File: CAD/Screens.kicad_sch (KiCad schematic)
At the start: 1 part

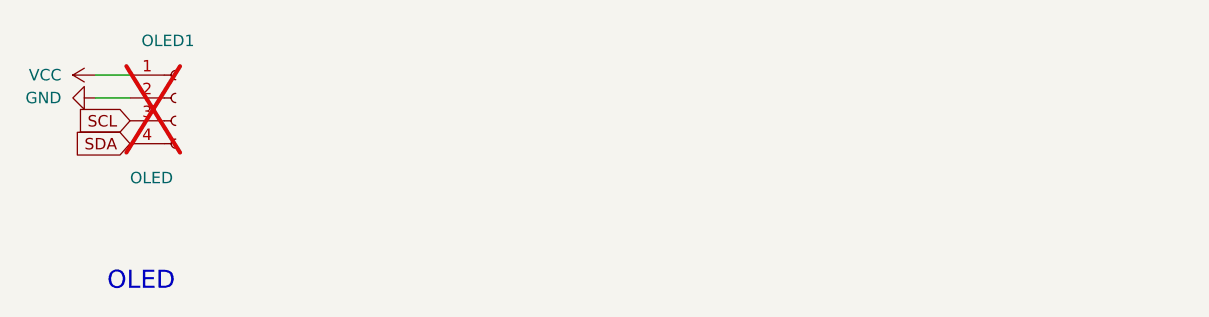
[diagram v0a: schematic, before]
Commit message: adding footprints and starting to route
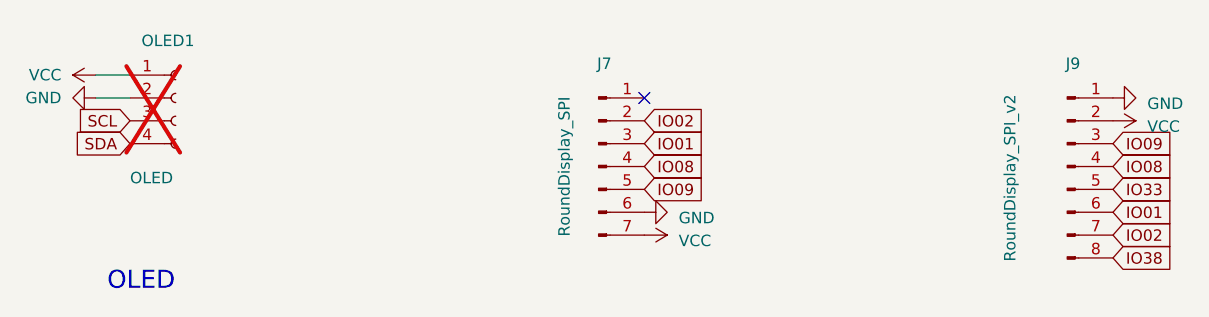
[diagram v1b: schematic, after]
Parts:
- added J7: RoundDisplay_SPI, Connector_PinSocket_2.54mm:PinSocket_1x07_P2.54mm_Vertical, symbol Connector:Conn_01x07_Pin
- added J9: RoundDisplay_SPI_v2, Connector_PinSocket_2.54mm:PinSocket_1x08_P2.54mm_Vertical, symbol Connector:Conn_01x08_Pin
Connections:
- net GND: now also J7.6 (Pin_6), J9.1 (Pin_1)
- net VCC: now also J7.7 (Pin_7), J9.2 (Pin_2)
- new net IO01: J7.3 (Pin_3), J9.6 (Pin_6)
- new net IO02: J7.2 (Pin_2), J9.7 (Pin_7)
- new net IO08: J7.4 (Pin_4), J9.4 (Pin_4)
- new net IO09: J7.5 (Pin_5), J9.3 (Pin_3)
- new net IO33: J9.5 (Pin_5)
- new net IO38: J9.8 (Pin_8)
- no-connect marks 0 -> 1
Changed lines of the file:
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@@
 (kicad_sch (version 20230121) (generator eeschema)
   (paper "A4")
+  (no_connect (at 133.35 69.85))
   (wire (pts (xy 72.39 67.31) (xy 76.2 67.31))
     (stroke (width 0) (type default))
@@
   (text "OLED" (at 73.66 91.44 0)
     (effects (font (size 2.0066 2.0066)) (justify left bottom))
+  )
+  (global_label "IO02" (shape input) (at 133.35 72.39 0) (fields_autoplaced)
+    (effects (font (size 1.27 1.27)) (justify left))
+    (property "Intersheetrefs" "${INTERSHEET_REFS}" (at 139.9559 72.39 0)
+      (effects (font (size 1.27 1.27)) (justify left) hide)
+    )
+  )
+  (global_label "IO38" (shape input) (at 185.42 87.63 0) (fields_autoplaced)
+    (effects (font (size 1.27 1.27)) (justify left))
+    (property "Intersheetrefs" "${INTERSHEET_REFS}" (at 192.0259 87.63 0)
+      (effects (font (size 1.27 1.27)) (justify left) hide)
+    )
+  )
+  (global_label "IO01" (shape input) (at 185.42 82.55 0) (fields_autoplaced)
+    (effects (font (size 1.27 1.27)) (justify left))
+    (property "Intersheetrefs" "${INTERSHEET_REFS}" (at 192.0259 82.55 0)
+      (effects (font (size 1.27 1.27)) (justify left) hide)
+    )
+  )
+  (global_label "IO09" (shape input) (at 185.42 74.93 0) (fields_autoplaced)
+    (effects (font (size 1.27 1.27)) (justify left))
+    (property "Intersheetrefs" "${INTERSHEET_REFS}" (at 192.0259 74.93 0)
+      (effects (font (size 1.27 1.27)) (justify left) hide)
+    )
   )
   (global_label "SDA" (shape input) (at 76.2 74.93 180) (fields_autoplaced)
@@
     )
   )
+  (global_label "IO08" (shape input) (at 133.35 77.47 0) (fields_autoplaced)
+    (effects (font (size 1.27 1.27)) (justify left))
+    (property "Intersheetrefs" "${INTERSHEET_REFS}" (at 139.9559 77.47 0)
+      (effects (font (size 1.27 1.27)) (justify left) hide)
+    )
+  )
+  (global_label "IO08" (shape input) (at 185.42 77.47 0) (fields_autoplaced)
+    (effects (font (size 1.27 1.27)) (justify left))
+    (property "Intersheetrefs" "${INTERSHEET_REFS}" (at 192.0259 77.47 0)
+      (effects (font (size 1.27 1.27)) (justify left) hide)
+    )
+  )
+  (global_label "IO01" (shape input) (at 133.35 74.93 0) (fields_autoplaced)
+    (effects (font (size 1.27 1.27)) (justify left))
+    (property "Intersheetrefs" "${INTERSHEET_REFS}" (at 139.9559 74.93 0)
+      (effects (font (size 1.27 1.27)) (justify left) hide)
+    )
+  )
   (global_label "SCL" (shape input) (at 76.2 72.39 180) (fields_autoplaced)
     (effects (font (size 1.27 1.27)) (justify right))
@@
     )
   )
+  (global_label "IO09" (shape input) (at 133.35 80.01 0) (fields_autoplaced)
+    (effects (font (size 1.27 1.27)) (justify left))
+    (property "Intersheetrefs" "${INTERSHEET_REFS}" (at 139.9559 80.01 0)
+      (effects (font (size 1.27 1.27)) (justify left) hide)
+    )
+  )
+  (global_label "IO33" (shape input) (at 185.42 80.01 0) (fields_autoplaced)
+    (effects (font (size 1.27 1.27)) (justify left))
+    (property "Intersheetrefs" "${INTERSHEET_REFS}" (at 192.0259 80.01 0)
+      (effects (font (size 1.27 1.27)) (justify left) hide)
+    )
+  )
+  (global_label "IO02" (shape input) (at 185.42 85.09 0) (fields_autoplaced)
+    (effects (font (size 1.27 1.27)) (justify left))
+    (property "Intersheetrefs" "${INTERSHEET_REFS}" (at 192.0259 85.09 0)
+      (effects (font (size 1.27 1.27)) (justify left) hide)
+    )
+  )
+  (symbol (lib_name "VCC_1") (lib_id "power:VCC") (at 185.42 72.39 270) (unit 1)
+    (in_bom yes) (on_board yes) (dnp no) (fields_autoplaced)
+    (property "Reference" "#PWR068" (at 181.61 72.39 0)
+      (effects (font (size 1.27 1.27)) hide)
+    )
+    (property "Value" "VCC" (at 189.23 73.025 90)
+      (effects (font (size 1.27 1.27)) (justify left))
+    )
+    (property "Footprint" "" (at 185.42 72.39 0)
+      (effects (font (size 1.27 1.27)) hide)
+    )
+    (property "Datasheet" "" (at 185.42 72.39 0)
+      (effects (font (size 1.27 1.27)) hide)
+    )
+    (pin "1")
+    (instances
+      (project "ProjectNeoRogue"
+        (path "/76a22395-5d2d-4f66-8191-432f65fdc4ac/7bbc5ee4-a356-48de-a261-211ab35ec87b"
+          (reference "#PWR068") (unit 1)
+        )
+      )
+    )
+  )
+  (symbol (lib_id "Connector:Conn_01x08_Pin") (at 180.34 77.47 0) (unit 1)
+    (in_bom yes) (on_board yes) (dnp no)
+    (property "Reference" "J9" (at 180.975 66.04 0)
+      (effects (font (size 1.27 1.27)))
+    )
+    (property "Value" "RoundDisplay_SPI_v2" (at 173.99 78.74 90)
+      (effects (font (size 1.27 1.27)))
+    )
+    (property "Footprint" "Connector_PinSocket_2.54mm:PinSocket_1x08_P2.54mm_Vertical" (at 180.34 77.47 0)
+      (effects (font (size 1.27 1.27)) hide)
+    )
+    (property "Datasheet" "~" (at 180.34 77.47 0)
+      (effects (font (size 1.27 1.27)) hide)
+    )
+    (pin "1")
+    (pin "2")
+    (pin "3")
+    (pin "4")
+    (pin "5")
+    (pin "6")
+    (pin "7")
+    (pin "8")
+    (instances
+      (project "ProjectNeoRogue"
+        (path "/76a22395-5d2d-4f66-8191-432f65fdc4ac/7bbc5ee4-a356-48de-a261-211ab35ec87b"
+          (reference "J9") (unit 1)
+        )
+      )
+    )
+  )
+  (symbol (lib_id "Connector:Conn_01x07_Pin") (at 128.27 77.47 0) (unit 1)
+    (in_bom yes) (on_board yes) (dnp no)
+    (property "Reference" "J7" (at 128.905 66.04 0)
+      (effects (font (size 1.27 1.27)))
+    )
+    (property "Value" "RoundDisplay_SPI" (at 124.46 77.47 90)
+      (effects (font (size 1.27 1.27)))
+    )
+    (property "Footprint" "Connector_PinSocket_2.54mm:PinSocket_1x07_P2.54mm_Vertical" (at 128.27 77.47 0)
+      (effects (font (size 1.27 1.27)) hide)
+    )
+    (property "Datasheet" "~" (at 128.27 77.47 0)
+      (effects (font (size 1.27 1.27)) hide)
+    )
+    (pin "1")
+    (pin "2")
+    (pin "3")
+    (pin "4")
+    (pin "5")
+    (pin "6")
+    (pin "7")
+    (instances
+      (project "ProjectNeoRogue"
+        (path "/76a22395-5d2d-4f66-8191-432f65fdc4ac/7bbc5ee4-a356-48de-a261-211ab35ec87b"
+          (reference "J7") (unit 1)
+        )
+      )
+    )
+  )
   (symbol (lib_id "power:GND") (at 72.39 69.85 270) (unit 1)
     (in_bom yes) (on_board yes) (dnp no) (fields_autoplaced)
@@
     )
   )
+  (symbol (lib_name "GND_1") (lib_id "power:GND") (at 133.35 82.55 90) (unit 1)
+    (in_bom yes) (on_board yes) (dnp no) (fields_autoplaced)
+    (property "Reference" "#PWR065" (at 139.7 82.55 0)
+      (effects (font (size 1.27 1.27)) hide)
+    )
+    (property "Value" "GND" (at 137.16 83.185 90)
+      (effects (font (size 1.27 1.27)) (justify right))
+    )
+    (property "Footprint" "" (at 133.35 82.55 0)
+      (effects (font (size 1.27 1.27)) hide)
+    )
+    (property "Datasheet" "" (at 133.35 82.55 0)
+      (effects (font (size 1.27 1.27)) hide)
+    )
+    (pin "1")
+    (instances
+      (project "ProjectNeoRogue"
+        (path "/76a22395-5d2d-4f66-8191-432f65fdc4ac/7bbc5ee4-a356-48de-a261-211ab35ec87b"
+          (reference "#PWR065") (unit 1)
+        )
+      )
+    )
+  )
   (symbol (lib_id "power:VCC") (at 72.39 67.31 90) (unit 1)
     (in_bom yes) (on_board yes) (dnp no) (fields_autoplaced)
@@
         )
       )
+    )
+  )
+  (symbol (lib_name "VCC_1") (lib_id "power:VCC") (at 133.35 85.09 270) (unit 1)
+    (in_bom yes) (on_board yes) (dnp no) (fields_autoplaced)
+    (property "Reference" "#PWR066" (at 129.54 85.09 0)
+      (effects (font (size 1.27 1.27)) hide)
+    )
+    (property "Value" "VCC" (at 137.16 85.725 90)
+      (effects (font (size 1.27 1.27)) (justify left))
+    )
+    (property "Footprint" "" (at 133.35 85.09 0)
+      (effects (font (size 1.27 1.27)) hide)
+    )
+    (property "Datasheet" "" (at 133.35 85.09 0)
+      (effects (font (size 1.27 1.27)) hide)
+    )
+    (pin "1")
+    (instances
+      (project "ProjectNeoRogue"
+        (path "/76a22395-5d2d-4f66-8191-432f65fdc4ac/7bbc5ee4-a356-48de-a261-211ab35ec87b"
+          (reference "#PWR066") (unit 1)
+        )
+      )
+    )
+  )
+  (symbol (lib_name "GND_1") (lib_id "power:GND") (at 185.42 69.85 90) (unit 1)
+    (in_bom yes) (on_board yes) (dnp no) (fields_autoplaced)
+    (property "Reference" "#PWR067" (at 191.77 69.85 0)
+      (effects (font (size 1.27 1.27)) hide)
+    )
+    (property "Value" "GND" (at 189.23 70.485 90)
+      (effects (font (size 1.27 1.27)) (justify right))
+    )
+    (property "Footprint" "" (at 185.42 69.85 0)
+      (effects (font (size 1.27 1.27)) hide)
+    )
+    (property "Datasheet" "" (at 185.42 69.85 0)
+      (effects (font (size 1.27 1.27)) hide)
+    )
+    (pin "1")
+    (instances
+      (project "ProjectNeoRogue"
+        (path "/76a22395-5d2d-4f66-8191-432f65fdc4ac/7bbc5ee4-a356-48de-a261-211ab35ec87b"
+          (reference "#PWR067") (unit 1)
+        )
+      )

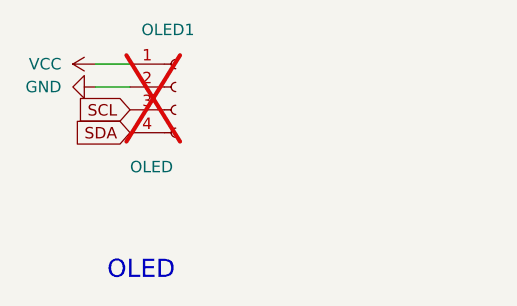
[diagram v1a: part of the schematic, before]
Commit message: routing and removing buttons OLED
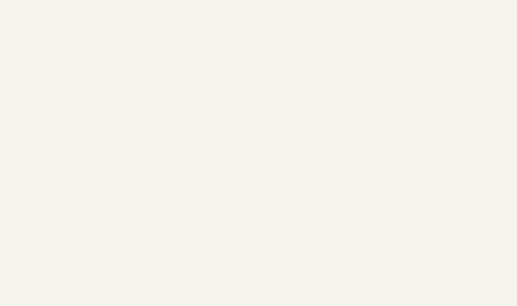
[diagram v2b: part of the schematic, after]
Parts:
- removed OLED1: OLED, Connector_PinHeader_2.54mm:PinHeader_1x04_P2.54mm_Vertical, symbol Connector:Conn_01x04_Female
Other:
- note removed: "OLED"
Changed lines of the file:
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@@
   (paper "A4")
   (no_connect (at 133.35 69.85))
-  (wire (pts (xy 72.39 67.31) (xy 76.2 67.31))
-    (stroke (width 0) (type default))
-  )
-  (wire (pts (xy 72.39 69.85) (xy 76.2 69.85))
-    (stroke (width 0) (type default))
-  )
-  (text "OLED" (at 73.66 91.44 0)
-    (effects (font (size 2.0066 2.0066)) (justify left bottom))
-  )
   (global_label "IO02" (shape input) (at 133.35 72.39 0) (fields_autoplaced)
     (effects (font (size 1.27 1.27)) (justify left))
@@
     )
   )
-  (global_label "SDA" (shape input) (at 76.2 74.93 180) (fields_autoplaced)
-    (effects (font (size 1.27 1.27)) (justify right))
-    (property "Intersheetrefs" "${INTERSHEET_REFS}" (at 70.2188 74.8506 0)
-      (effects (font (size 1.27 1.27)) (justify right) hide)
-    )
-  )
   (global_label "IO08" (shape input) (at 133.35 77.47 0) (fields_autoplaced)
     (effects (font (size 1.27 1.27)) (justify left))
@@
     (property "Intersheetrefs" "${INTERSHEET_REFS}" (at 139.9559 74.93 0)
       (effects (font (size 1.27 1.27)) (justify left) hide)
-    )
-  )
-  (global_label "SCL" (shape input) (at 76.2 72.39 180) (fields_autoplaced)
-    (effects (font (size 1.27 1.27)) (justify right))
-    (property "Intersheetrefs" "${INTERSHEET_REFS}" (at 70.2793 72.3106 0)
-      (effects (font (size 1.27 1.27)) (justify right) hide)
     )
   )
@@
     )
   )
-  (symbol (lib_id "power:GND") (at 72.39 69.85 270) (unit 1)
-    (in_bom yes) (on_board yes) (dnp no) (fields_autoplaced)
-    (property "Reference" "#PWR023" (at 66.04 69.85 0)
-      (effects (font (size 1.27 1.27)) hide)
-    )
-    (property "Value" "GND" (at 68.58 69.8499 90)
-      (effects (font (size 1.27 1.27)) (justify right))
-    )
-    (property "Footprint" "" (at 72.39 69.85 0)
-      (effects (font (size 1.27 1.27)) hide)
-    )
-    (property "Datasheet" "" (at 72.39 69.85 0)
-      (effects (font (size 1.27 1.27)) hide)
-    )
-    (pin "1")
-    (instances
-      (project "ProjectNeoRogue"
-        (path "/76a22395-5d2d-4f66-8191-432f65fdc4ac"
-          (reference "#PWR023") (unit 1)
-        )
-        (path "/76a22395-5d2d-4f66-8191-432f65fdc4ac/7bbc5ee4-a356-48de-a261-211ab35ec87b"
-          (reference "#PWR023") (unit 1)
-        )
-      )
-    )
-  )
-  (symbol (lib_id "Connector:Conn_01x04_Female") (at 81.28 69.85 0) (unit 1)
-    (in_bom no) (on_board yes) (dnp yes)
-    (property "Reference" "OLED1" (at 77.47 63.5 0)
-      (effects (font (size 1.27 1.27)) (justify left))
-    )
-    (property "Value" "OLED" (at 76.2 78.74 0)
-      (effects (font (size 1.27 1.27)) (justify left))
-    )
-    (property "Footprint" "Connector_PinHeader_2.54mm:PinHeader_1x04_P2.54mm_Vertical" (at 81.28 69.85 0)
-      (effects (font (size 1.27 1.27)) hide)
-    )
-    (property "Datasheet" "~" (at 81.28 69.85 0)
-      (effects (font (size 1.27 1.27)) hide)
-    )
-    (property "OrderURL" "" (at 81.28 69.85 0)
-      (effects (font (size 1.27 1.27)) hide)
-    )
-    (pin "1")
-    (pin "2")
-    (pin "3")
-    (pin "4")
-    (instances
-      (project "ProjectNeoRogue"
-        (path "/76a22395-5d2d-4f66-8191-432f65fdc4ac"
-          (reference "OLED1") (unit 1)
-        )
-        (path "/76a22395-5d2d-4f66-8191-432f65fdc4ac/7bbc5ee4-a356-48de-a261-211ab35ec87b"
-          (reference "OLED1") (unit 1)
-        )
-      )
-    )
-  )
   (symbol (lib_name "GND_1") (lib_id "power:GND") (at 133.35 82.55 90) (unit 1)
     (in_bom yes) (on_board yes) (dnp no) (fields_autoplaced)
@@
         )
       )
-    )
-  )
-  (symbol (lib_id "power:VCC") (at 72.39 67.31 90) (unit 1)
-    (in_bom yes) (on_board yes) (dnp no) (fields_autoplaced)
-    (property "Reference" "#PWR022" (at 76.2 67.31 0)
-      (effects (font (size 1.27 1.27)) hide)
-    )
-    (property "Value" "VCC" (at 68.58 67.3099 90)
-      (effects (font (size 1.27 1.27)) (justify left))
-    )
-    (property "Footprint" "" (at 72.39 67.31 0)
-      (effects (font (size 1.27 1.27)) hide)
-    )
-    (property "Datasheet" "" (at 72.39 67.31 0)
-      (effects (font (size 1.27 1.27)) hide)
-    )
-    (pin "1")
-    (instances
-      (project "ProjectNeoRogue"
-        (path "/76a22395-5d2d-4f66-8191-432f65fdc4ac"
-          (reference "#PWR022") (unit 1)
-        )
-        (path "/76a22395-5d2d-4f66-8191-432f65fdc4ac/7bbc5ee4-a356-48de-a261-211ab35ec87b"
-          (reference "#PWR022") (unit 1)
-        )
-      )

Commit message: Updated pins and moar
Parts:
- added R25 (x2): 4.7k, BadgePirates:R_1206_3216Metric, symbol Device:R_Small_US
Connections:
- net IO08: now also R25.2
- net IO09: now also R25.2
- net VCC: now also R25.1, R25.1
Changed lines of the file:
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@@
 (kicad_sch (version 20230121) (generator eeschema)
   (paper "A4")
+  (junction (at 153.67 80.01) (diameter 0) (color 0 0 0 0)
+  )
+  (junction (at 144.78 77.47) (diameter 0) (color 0 0 0 0)
+  )
   (no_connect (at 133.35 69.85))
+  (wire (pts (xy 153.67 66.675) (xy 153.67 69.85))
+    (stroke (width 0) (type default))
+  )
+  (wire (pts (xy 144.78 75.565) (xy 144.78 77.47))
+    (stroke (width 0) (type default))
+  )
+  (wire (pts (xy 153.67 74.93) (xy 153.67 80.01))
+    (stroke (width 0) (type default))
+  )
+  (wire (pts (xy 144.78 67.31) (xy 144.78 70.485))
+    (stroke (width 0) (type default))
+  )
+  (wire (pts (xy 153.67 80.01) (xy 133.35 80.01))
+    (stroke (width 0) (type default))
+  )
+  (wire (pts (xy 158.115 80.01) (xy 153.67 80.01))
+    (stroke (width 0) (type default))
+  )
+  (wire (pts (xy 144.78 77.47) (xy 133.35 77.47))
+    (stroke (width 0) (type default))
+  )
+  (wire (pts (xy 158.115 77.47) (xy 144.78 77.47))
+    (stroke (width 0) (type default))
+  )
   (global_label "IO02" (shape input) (at 133.35 72.39 0) (fields_autoplaced)
     (effects (font (size 1.27 1.27)) (justify left))
@@
     )
   )
-  (global_label "IO08" (shape input) (at 133.35 77.47 0) (fields_autoplaced)
-    (effects (font (size 1.27 1.27)) (justify left))
-    (property "Intersheetrefs" "${INTERSHEET_REFS}" (at 139.9559 77.47 0)
+  (global_label "IO08" (shape input) (at 158.115 77.47 0) (fields_autoplaced)
+    (effects (font (size 1.27 1.27)) (justify left))
+    (property "Intersheetrefs" "${INTERSHEET_REFS}" (at 164.7209 77.47 0)
       (effects (font (size 1.27 1.27)) (justify left) hide)
     )
@@
     )
   )
-  (global_label "IO09" (shape input) (at 133.35 80.01 0) (fields_autoplaced)
-    (effects (font (size 1.27 1.27)) (justify left))
-    (property "Intersheetrefs" "${INTERSHEET_REFS}" (at 139.9559 80.01 0)
+  (global_label "IO09" (shape input) (at 158.115 80.01 0) (fields_autoplaced)
+    (effects (font (size 1.27 1.27)) (justify left))
+    (property "Intersheetrefs" "${INTERSHEET_REFS}" (at 164.7209 80.01 0)
       (effects (font (size 1.27 1.27)) (justify left) hide)
     )
@@
         (path "/76a22395-5d2d-4f66-8191-432f65fdc4ac/7bbc5ee4-a356-48de-a261-211ab35ec87b"
           (reference "#PWR068") (unit 1)
+        )
+      )
+    )
+  )
+  (symbol (lib_id "power:VCC") (at 144.78 67.31 0) (unit 1)
+    (in_bom yes) (on_board yes) (dnp no)
+    (property "Reference" "#PWR027" (at 144.78 71.12 0)
+      (effects (font (size 1.27 1.27)) hide)
+    )
+    (property "Value" "VCC" (at 145.161 62.9158 0)
+      (effects (font (size 1.27 1.27)))
+    )
+    (property "Footprint" "" (at 144.78 67.31 0)
+      (effects (font (size 1.27 1.27)) hide)
+    )
+    (property "Datasheet" "" (at 144.78 67.31 0)
+      (effects (font (size 1.27 1.27)) hide)
+    )
+    (pin "1")
+    (instances
+      (project "ProjectNeoRogue"
+        (path "/76a22395-5d2d-4f66-8191-432f65fdc4ac"
+          (reference "#PWR027") (unit 1)
+        )
+        (path "/76a22395-5d2d-4f66-8191-432f65fdc4ac/7bbc5ee4-a356-48de-a261-211ab35ec87b"
+          (reference "#PWR028") (unit 1)
         )
       )
@@
     )
   )
+  (symbol (lib_id "Device:R_Small_US") (at 153.67 72.39 0) (unit 1)
+    (in_bom yes) (on_board yes) (dnp no)
+    (property "Reference" "R25" (at 155.3972 71.2216 0)
+      (effects (font (size 1.27 1.27)) (justify left))
+    )
+    (property "Value" "4.7k" (at 155.3972 73.533 0)
+      (effects (font (size 1.27 1.27)) (justify left))
+    )
+    (property "Footprint" "BadgePirates:R_1206_3216Metric" (at 153.67 72.39 0)
+      (effects (font (size 1.27 1.27)) hide)
+    )
+    (property "Datasheet" "~" (at 153.67 72.39 0)
+      (effects (font (size 1.27 1.27)) hide)
+    )
+    (property "OrderURL" "" (at 153.67 72.39 0)
+      (effects (font (size 1.27 1.27)) hide)
+    )
+    (pin "1")
+    (pin "2")
+    (instances
+      (project "ProjectNeoRogue"
+        (path "/76a22395-5d2d-4f66-8191-432f65fdc4ac"
+          (reference "R25") (unit 1)
+        )
+        (path "/76a22395-5d2d-4f66-8191-432f65fdc4ac/7bbc5ee4-a356-48de-a261-211ab35ec87b"
+          (reference "R27") (unit 1)
+        )
+      )
+    )
+  )
+  (symbol (lib_id "Device:R_Small_US") (at 144.78 73.025 0) (unit 1)
+    (in_bom yes) (on_board yes) (dnp no)
+    (property "Reference" "R25" (at 146.5072 71.8566 0)
+      (effects (font (size 1.27 1.27)) (justify left))
+    )
+    (property "Value" "4.7k" (at 146.5072 74.168 0)
+      (effects (font (size 1.27 1.27)) (justify left))
+    )
+    (property "Footprint" "BadgePirates:R_1206_3216Metric" (at 144.78 73.025 0)
+      (effects (font (size 1.27 1.27)) hide)
+    )
+    (property "Datasheet" "~" (at 144.78 73.025 0)
+      (effects (font (size 1.27 1.27)) hide)
+    )
+    (property "OrderURL" "" (at 144.78 73.025 0)
+      (effects (font (size 1.27 1.27)) hide)
+    )
+    (pin "1")
+    (pin "2")
+    (instances
+      (project "ProjectNeoRogue"
+        (path "/76a22395-5d2d-4f66-8191-432f65fdc4ac"
+          (reference "R25") (unit 1)
+        )
+        (path "/76a22395-5d2d-4f66-8191-432f65fdc4ac/7bbc5ee4-a356-48de-a261-211ab35ec87b"
+          (reference "R23") (unit 1)
+        )
+      )
+    )
+  )
   (symbol (lib_name "GND_1") (lib_id "power:GND") (at 133.35 82.55 90) (unit 1)
     (in_bom yes) (on_board yes) (dnp no) (fields_autoplaced)
@@
         )
       )
+    )
+  )
+  (symbol (lib_id "power:VCC") (at 153.67 66.675 0) (unit 1)
+    (in_bom yes) (on_board yes) (dnp no)
+    (property "Reference" "#PWR027" (at 153.67 70.485 0)
+      (effects (font (size 1.27 1.27)) hide)
+    )
+    (property "Value" "VCC" (at 154.051 62.2808 0)
+      (effects (font (size 1.27 1.27)))
+    )
+    (property "Footprint" "" (at 153.67 66.675 0)
+      (effects (font (size 1.27 1.27)) hide)
+    )
+    (property "Datasheet" "" (at 153.67 66.675 0)
+      (effects (font (size 1.27 1.27)) hide)
+    )
+    (pin "1")
+    (instances
+      (project "ProjectNeoRogue"
+        (path "/76a22395-5d2d-4f66-8191-432f65fdc4ac"
+          (reference "#PWR027") (unit 1)
+        )
+        (path "/76a22395-5d2d-4f66-8191-432f65fdc4ac/7bbc5ee4-a356-48de-a261-211ab35ec87b"
+          (reference "#PWR032") (unit 1)
+        )
+      )
